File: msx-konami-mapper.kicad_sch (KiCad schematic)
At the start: 1 part, among them U1 SST39SF040

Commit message: Edge connector
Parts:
- added U2: ~, MSX:Cartridge, symbol MSX:Cartridge
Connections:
- new net +5V: U2.45 (+5V), U2.47 (+5V)
- new net GND: U2.41 (GND), U2.43 (GND)
- no-connect marks 0 -> 2

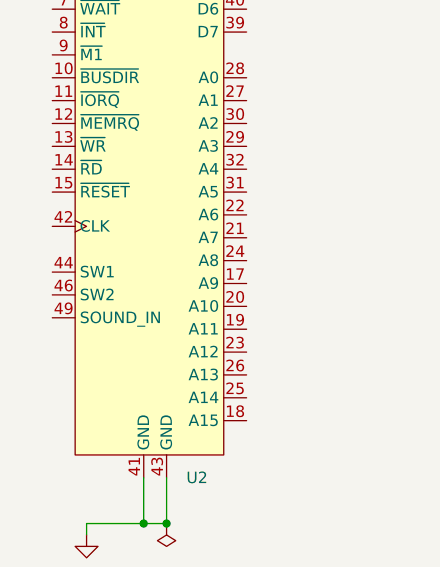
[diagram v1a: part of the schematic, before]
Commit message: Put the connector the right way around, dimwit
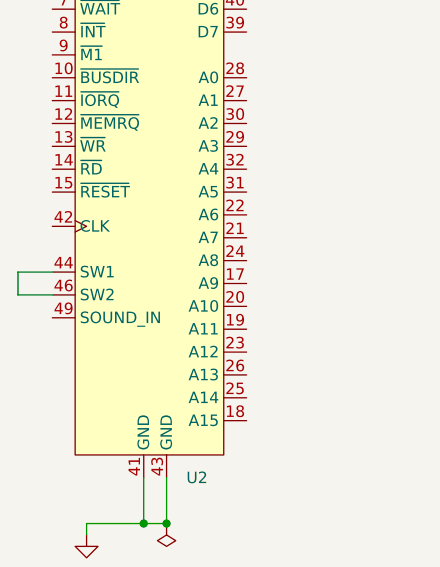
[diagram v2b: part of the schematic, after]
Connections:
- net at U2.44 (SW1): now also U2.46 (SW2)
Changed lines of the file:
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@@
+	(wire
+		(pts
+			(xy 34.29 127) (xy 38.1 127)
+		)
+		(stroke
+			(width 0)
+			(type default)
+		)
+	)
 	(wire
 		(pts
@@
 	(wire
 		(pts
+			(xy 34.29 124.46) (xy 34.29 127)
+		)
+		(stroke
+			(width 0)
+			(type default)
+		)
+	)
+	(wire
+		(pts
 			(xy 48.26 68.58) (xy 45.72 68.58)
 		)
@@
 		)
 		(stroke
+			(width 0)
+			(type default)
+		)
+	)
+	(wire
+		(pts
+			(xy 38.1 124.46) (xy 34.29 124.46)
+		)
+		(stroke

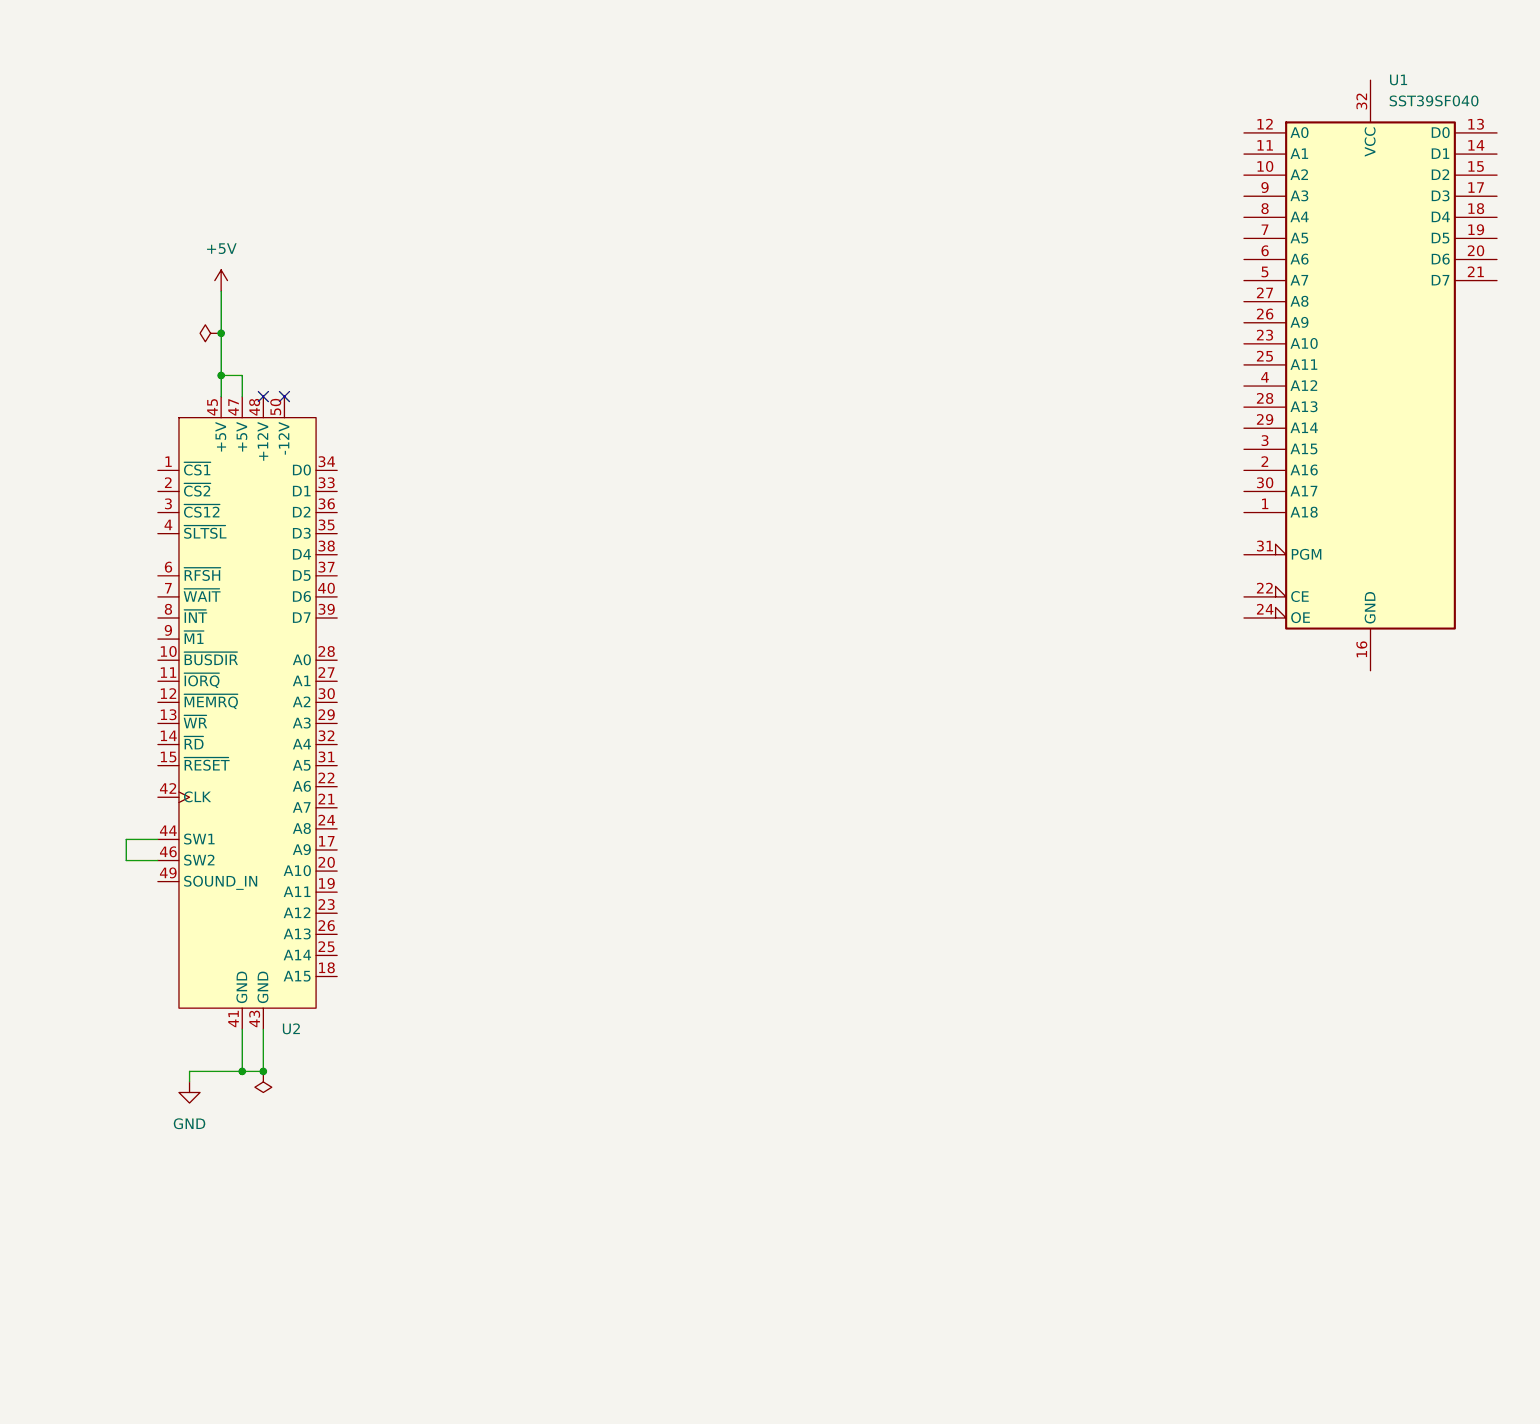
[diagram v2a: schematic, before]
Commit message: Data pins
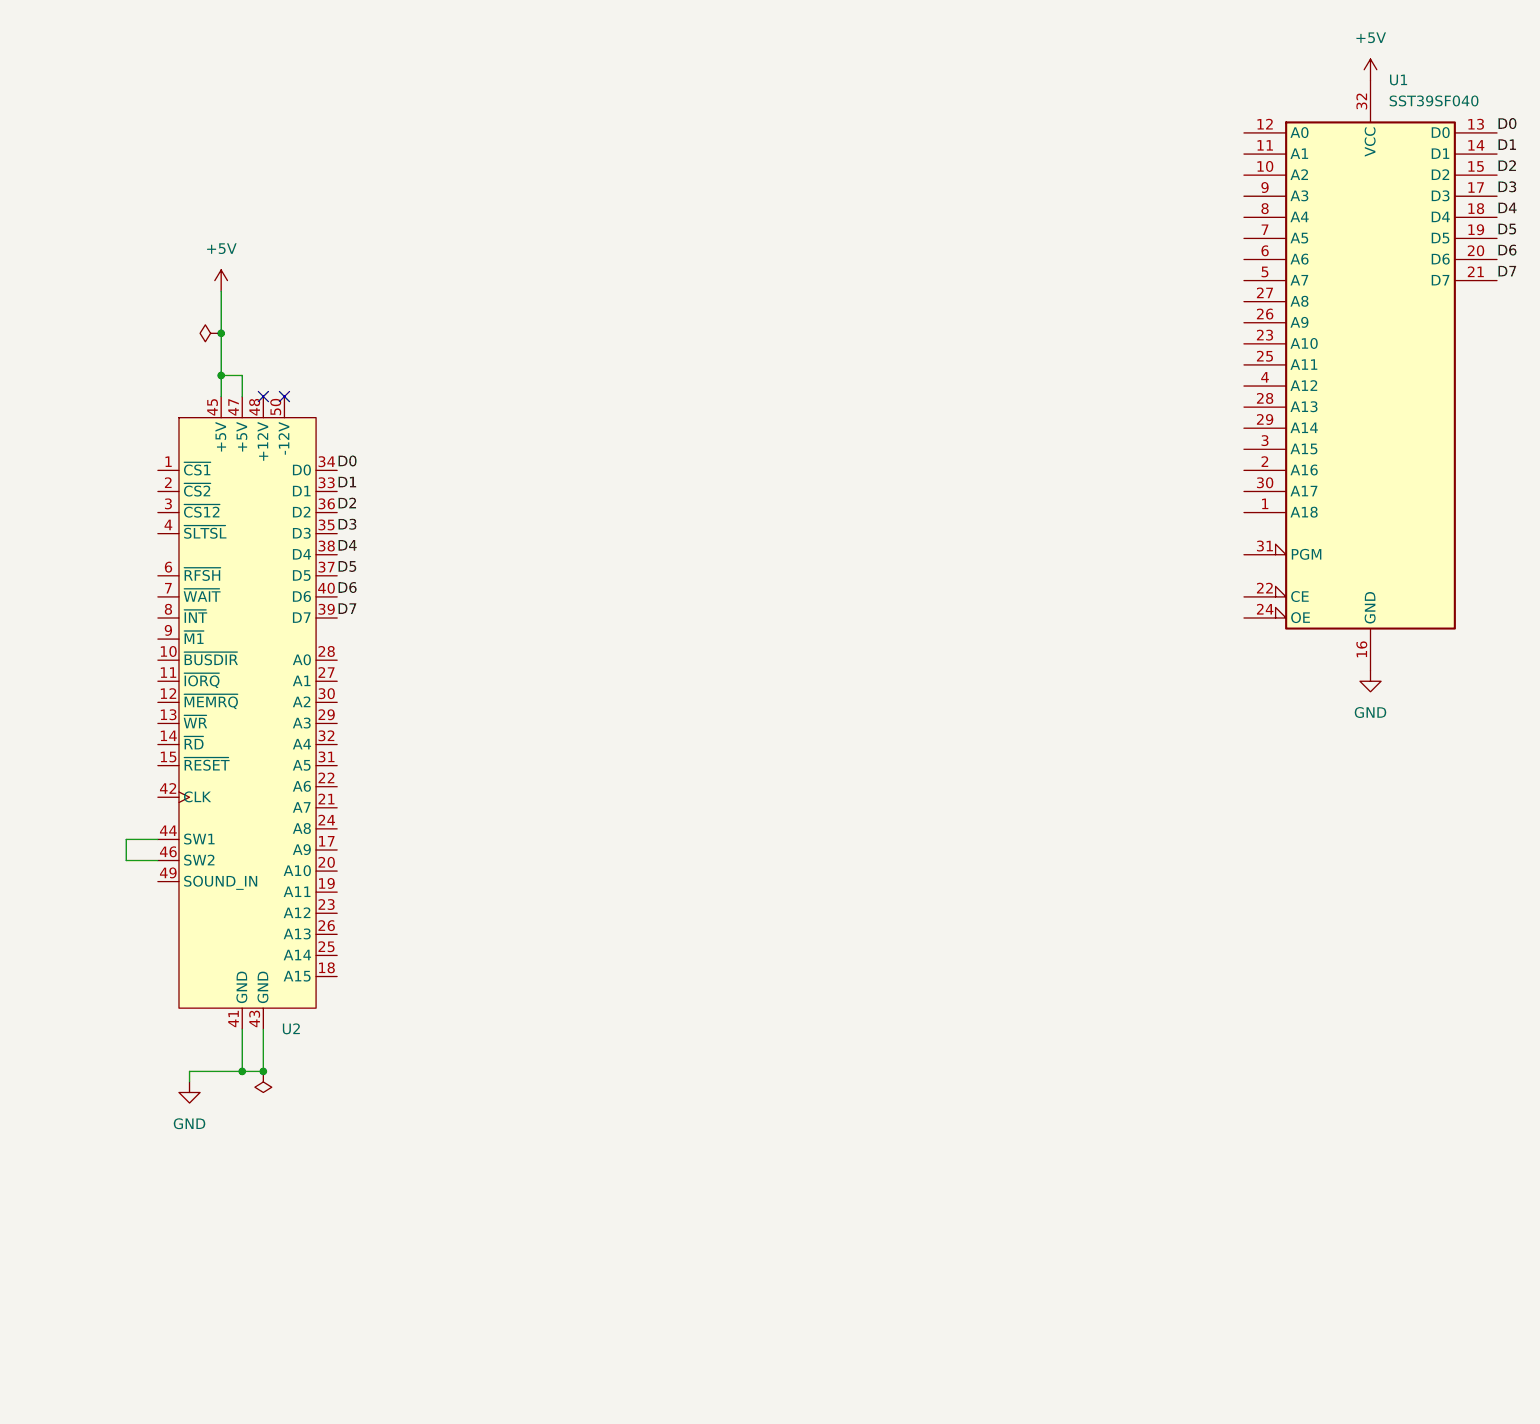
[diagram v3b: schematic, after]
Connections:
- net +5V: now also U1.32 (VCC)
- net GND: now also U1.16 (GND)
- net D1: now reaches U2.33 (D1)
- net D1: now also U1.14 (D1)
- net D0: now reaches U2.34 (D0)
- net D0: now also U1.13 (D0)
- net D3: now reaches U2.35 (D3)
- net D3: now also U1.17 (D3)
- net D2: now reaches U2.36 (D2)
- net D2: now also U1.15 (D2)
- net D5: now reaches U2.37 (D5)
- net D5: now also U1.19 (D5)
- net D4: now reaches U2.38 (D4)
- net D4: now also U1.18 (D4)
- net D7: now reaches U2.39 (D7)
- net D7: now also U1.21 (D7)
- net D6: now reaches U2.40 (D6)
- net D6: now also U1.20 (D6)

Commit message: Disable programming for v1.0
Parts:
- added JP1: Jumper_2_Bridged, Jumper:SolderJumper-2_P1.3mm_Bridged_Pad1.0x1.5mm, symbol Jumper:Jumper_2_Bridged
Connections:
- net +5V: now also JP1.1 (A)
- net at U1.31 (PGM): now also JP1.2 (B)
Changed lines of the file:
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@@
+	(wire
+		(pts
+			(xy 149.86 90.17) (xy 158.75 90.17)
+		)
+		(stroke
+			(width 0)
+			(type default)
+		)
+	)
 	(wire
 		(pts
@@
 	(label "D7"
 		(at 59.69 97.79 0)
+		(fields_autoplaced yes)
 		(effects
 			(font
@@
 	(label "D5"
 		(at 59.69 92.71 0)
+		(fields_autoplaced yes)
 		(effects
 			(font
@@
 	(label "D3"
 		(at 59.69 87.63 0)
+		(fields_autoplaced yes)
 		(effects
 			(font
@@
 	(label "D1"
 		(at 199.39 41.91 0)
+		(fields_autoplaced yes)
 		(effects
 			(font
@@
 	(label "D4"
 		(at 59.69 90.17 0)
+		(fields_autoplaced yes)
 		(effects
 			(font
@@
 	(label "D5"
 		(at 199.39 52.07 0)
+		(fields_autoplaced yes)
 		(effects
 			(font
@@
 	(label "D6"
 		(at 59.69 95.25 0)
+		(fields_autoplaced yes)
 		(effects
 			(font
@@
 	(label "D6"
 		(at 199.39 54.61 0)
+		(fields_autoplaced yes)
 		(effects
 			(font
@@
 	(label "D0"
 		(at 199.39 39.37 0)
+		(fields_autoplaced yes)
 		(effects
 			(font
@@
 	(label "D0"
 		(at 59.69 80.01 0)
+		(fields_autoplaced yes)
 		(effects
 			(font
@@
 	(label "D4"
 		(at 199.39 49.53 0)
+		(fields_autoplaced yes)
 		(effects
 			(font
@@
 	(label "D7"
 		(at 199.39 57.15 0)
+		(fields_autoplaced yes)
 		(effects
 			(font
@@
 	(label "D2"
 		(at 199.39 44.45 0)
+		(fields_autoplaced yes)
 		(effects
 			(font
@@
 	(label "D2"
 		(at 59.69 85.09 0)
+		(fields_autoplaced yes)
 		(effects
 			(font
@@
 	(label "D1"
 		(at 59.69 82.55 0)
+		(fields_autoplaced yes)
 		(effects
 			(font
@@
 	(label "D3"
 		(at 199.39 46.99 0)
-		(effects
-			(font
-				(size 1.27 1.27)
-			)
-			(justify left bottom)
+		(fields_autoplaced yes)
+		(effects
+			(font
+				(size 1.27 1.27)
+			)
+			(justify left bottom)
+		)
+	)
+	(symbol
+		(lib_id "Jumper:Jumper_2_Bridged")
+		(at 163.83 90.17 0)
+		(unit 1)
+		(exclude_from_sim yes)
+		(in_bom yes)
+		(on_board yes)
+		(dnp no)
+		(fields_autoplaced yes)
+		(property "Reference" "JP1"
+			(at 163.83 87.63 0)
+			(effects
+				(font
+					(size 1.27 1.27)
+				)
+			)
+		)
+		(property "Value" "Jumper_2_Bridged"
+			(at 163.83 87.63 0)
+			(effects
+				(font
+					(size 1.27 1.27)
+				)
+				(hide yes)
+			)
+		)
+		(property "Footprint" "Jumper:SolderJumper-2_P1.3mm_Bridged_Pad1.0x1.5mm"
+			(at 163.83 90.17 0)
+			(effects
+				(font
+					(size 1.27 1.27)
+				)
+				(hide yes)
+			)
+		)
+		(property "Datasheet" "~"
+			(at 163.83 90.17 0)
+			(effects
+				(font
+					(size 1.27 1.27)
+				)
+				(hide yes)
+			)
+		)
+		(property "Description" "Jumper, 2-pole, closed/bridged"
+			(at 163.83 90.17 0)
+			(effects
+				(font
+					(size 1.27 1.27)
+				)
+				(hide yes)
+			)
+		)
+		(pin "1"
+		)
+		(pin "2"
+		)
+		(instances
+			(project ""
+				(path "/3ac3ee82-802b-4f0f-99fb-f88e392aa8f2"
+					(reference "JP1")
+					(unit 1)
+				)
+			)
 		)
 	)
@@
 					(unit 1)
 				)
+			)
+		)
+	)
+	(symbol
+		(lib_id "power:+5V")
+		(at 149.86 90.17 0)
+		(unit 1)
+		(exclude_from_sim no)
+		(in_bom yes)
+		(on_board yes)
+		(dnp no)
+		(fields_autoplaced yes)
+		(property "Reference" "#PWR05"
+			(at 149.86 93.98 0)
+			(effects
+				(font
+					(size 1.27 1.27)
+				)
+				(hide yes)
+			)
+		)
+		(property "Value" "+5V"
+			(at 149.86 85.09 0)
+			(effects
+				(font
+					(size 1.27 1.27)
+				)
+			)
+		)
+		(property "Footprint" ""
+			(at 149.86 90.17 0)
+			(effects
+				(font
+					(size 1.27 1.27)
+				)
+				(hide yes)
+			)
+		)
+		(property "Datasheet" ""
+			(at 149.86 90.17 0)
+			(effects
+				(font
+					(size 1.27 1.27)
+				)
+				(hide yes)
+			)
+		)
+		(property "Description" "Power symbol creates a global label with name \"+5V\""
+			(at 149.86 90.17 0)
+			(effects
+				(font
+					(size 1.27 1.27)
+				)
+				(hide yes)
+			)
+		)
+		(pin "1"
+		)
+		(instances
+			(project ""
+				(path "/3ac3ee82-802b-4f0f-99fb-f88e392aa8f2"
+					(reference "#PWR05")
+					(unit 1)
+				)

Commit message: The mysteries of decoding
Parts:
- added U3: 74LS670, Package_DIP:DIP-16_W7.62mm_Socket_LongPads, symbol 74xx:74LS670
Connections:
- net +5V: now also U3.16 (VCC)
- net GND: now also U3.8 (GND)
- no-connect marks 2 -> 3
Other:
- note added: "$4000-7fff"
- note added: "$4000-bfff"
- note added: "$8000-bfff"
- note added: "(Everything needs ~{SLTSEL}) Page 0: A14 Page 1: A13 + A14 Page 2: A15 Page 3: A13 + A15 How to deal with mirrors? How to do the 2-bit selection?"
- note added: "Page (8kB) Switching address Initial segment 4000h~5FFFh (mirror: C000h~DFFFh) None Always 0 6000h~7FFFh (mirror: E000h~FFFFh) 6000h (mirrors: 6001h~7FFFh) 1 8000h~9FFFh (mirror: 0000h~1FFFh) 8000h (mirrors: 8001h~9FFFh) Random A000h~BFFFh (mirror: 2000h~3FFFh) A000h (mirrors: A001h~BFFFh) Random"
- note added: "Read address"
- note added: "Write address"

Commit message: Starting to puzzle this out
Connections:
- net A9: now reaches U2.17 (A9)
- net A9: now also U1.26 (A9)
- net A11: now reaches U2.19 (A11)
- net A11: now also U1.25 (A11)
- net A10: now reaches U2.20 (A10)
- net A10: now also U1.23 (A10)
- net A7: now reaches U2.21 (A7)
- net A7: now also U1.5 (A7)
- net A6: now reaches U2.22 (A6)
- net A6: now also U1.6 (A6)
- net A12: now reaches U2.23 (A12)
- net A12: now also U1.4 (A12)
- net A8: now reaches U2.24 (A8)
- net A8: now also U1.27 (A8)
- net A13: now reaches U2.26 (A13)
- net A13: now also U1.28 (A13)
- net A1: now reaches U2.27 (A1)
- net A1: now also U1.11 (A1)
- net A0: now reaches U2.28 (A0)
- net A0: now also U1.12 (A0)
- net A3: now reaches U2.29 (A3)
- net A3: now also U1.9 (A3)
- net A2: now reaches U2.30 (A2)
- net A2: now also U1.10 (A2)
- net A5: now reaches U2.31 (A5)
- net A5: now also U1.7 (A5)
- net A4: now reaches U2.32 (A4)
- net A4: now also U1.8 (A4)
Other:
- note added: "Address within 8K page"

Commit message: Notes to self
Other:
- note added: "(Everything needs ~{SLTSEL}) Page 0: A14 Page 1: A13 + A14 Page 2: A15 Page 3: A13 + A15 How to deal with mirrors? How to do the 2-bit selection? (at least we can reuse some decode logic, it is the same switching address as the page space)"
- note removed: "(Everything needs ~{SLTSEL}) Page 0: A14 Page 1: A13 + A14 Page 2: A15 Page 3: A13 + A15 How to deal with mirrors? How to do the 2-bit selection?"
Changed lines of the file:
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@@
 		)
 	)
-	(text "(Everything needs ~{SLTSEL})\nPage 0: A14\nPage 1: A13 + A14\nPage 2: A15\nPage 3: A13 + A15\nHow to deal with mirrors?\nHow to do the 2-bit selection?"
+	(text "(Everything needs ~{SLTSEL})\nPage 0: A14\nPage 1: A13 + A14\nPage 2: A15\nPage 3: A13 + A15\nHow to deal with mirrors?\nHow to do the 2-bit selection?\n (at least we can reuse some decode logic, it is the same switching address as the page space)"
 		(exclude_from_sim no)
 		(at 21.844 165.1 0)
@@
 	(label "A0"
 		(at 168.91 39.37 180)
+		(fields_autoplaced yes)
 		(effects
 			(font
@@
 	(label "A1"
 		(at 168.91 41.91 180)
+		(fields_autoplaced yes)
 		(effects
 			(font
@@
 	(label "A13"
 		(at 59.69 135.89 0)
+		(fields_autoplaced yes)
 		(effects
 			(font
@@
 	(label "A1"
 		(at 59.69 105.41 0)
+		(fields_autoplaced yes)
 		(effects
 			(font
@@
 	(label "A6"
 		(at 59.69 118.11 0)
+		(fields_autoplaced yes)
 		(effects
 			(font
@@
 	(label "A5"
 		(at 168.91 52.07 180)
+		(fields_autoplaced yes)
 		(effects
 			(font
@@
 	(label "A12"
 		(at 59.69 133.35 0)
+		(fields_autoplaced yes)
 		(effects
 			(font
@@
 	(label "A4"
 		(at 168.91 49.53 180)
+		(fields_autoplaced yes)
 		(effects
 			(font
@@
 	(label "A2"
 		(at 168.91 44.45 180)
+		(fields_autoplaced yes)
 		(effects
 			(font
@@
 	(label "A5"
 		(at 59.69 115.57 0)
+		(fields_autoplaced yes)
 		(effects
 			(font
@@
 	(label "A12"
 		(at 168.91 69.85 180)
+		(fields_autoplaced yes)
 		(effects
 			(font
@@
 	(label "A3"
 		(at 168.91 46.99 180)
+		(fields_autoplaced yes)
 		(effects
 			(font
@@
 	(label "A3"
 		(at 59.69 110.49 0)
+		(fields_autoplaced yes)
 		(effects
 			(font
@@
 	(label "A11"
 		(at 59.69 130.81 0)
+		(fields_autoplaced yes)
 		(effects
 			(font
@@
 	(label "A8"
 		(at 59.69 123.19 0)
+		(fields_autoplaced yes)
 		(effects
 			(font
@@
 	(label "A9"
 		(at 59.69 125.73 0)
+		(fields_autoplaced yes)
 		(effects
 			(font
@@
 	(label "A6"
 		(at 168.91 54.61 180)
+		(fields_autoplaced yes)
 		(effects
 			(font
@@
 	(label "A4"
 		(at 59.69 113.03 0)
+		(fields_autoplaced yes)
 		(effects
 			(font
@@
 	(label "A8"
 		(at 168.91 59.69 180)
+		(fields_autoplaced yes)
 		(effects
 			(font
@@
 	(label "A7"
 		(at 168.91 57.15 180)
+		(fields_autoplaced yes)
 		(effects
 			(font
@@
 	(label "A7"
 		(at 59.69 120.65 0)
+		(fields_autoplaced yes)
 		(effects
 			(font
@@
 	(label "A0"
 		(at 59.69 102.87 0)
+		(fields_autoplaced yes)
 		(effects
 			(font
@@
 	(label "A13"
 		(at 168.91 72.39 180)
+		(fields_autoplaced yes)
 		(effects
 			(font
@@
 	(label "A9"
 		(at 168.91 62.23 180)
+		(fields_autoplaced yes)
 		(effects
 			(font
@@
 	(label "A2"
 		(at 59.69 107.95 0)
+		(fields_autoplaced yes)
 		(effects
 			(font
@@
 	(label "A10"
 		(at 168.91 64.77 180)
+		(fields_autoplaced yes)
 		(effects
 			(font
@@
 	(label "A10"
 		(at 59.69 128.27 0)
+		(fields_autoplaced yes)
 		(effects
 			(font
@@
 	(label "A11"
 		(at 168.91 67.31 180)
-		(effects
-			(font
+		(fields_autoplaced yes)
+		(effects
+			(font

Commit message: Experimental dual-game select
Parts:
- added SW1: High/Low, Connector_PinHeader_2.54mm:PinHeader_1x03_P2.54mm_Vertical, symbol Switch:SW_SPDT
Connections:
- net +5V: now also SW1.1 (A)
- net A13: no longer U1.28 (A13)
- net GND: now also SW1.3 (C)
- net PA18: now reaches U1.1 (A18)
- net PA18: now also SW1.2 (B)
- net PA16: now reaches U1.2 (A16)
- net PA14: now reaches U1.29 (A14)
- net PA15: now reaches U1.3 (A15)
- net PA17: now reaches U1.30 (A17)
- new net PA13: U1.28 (A13)
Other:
- note added: "Original mapper: 32 pages of 8 (5 bits of pages) = 256K 4Mbit ROM says: 512K. This toggle can be used to load two different games onto the ROM"
- note added: "Paged addresses"
